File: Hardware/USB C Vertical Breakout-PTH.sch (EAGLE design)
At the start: 15 parts

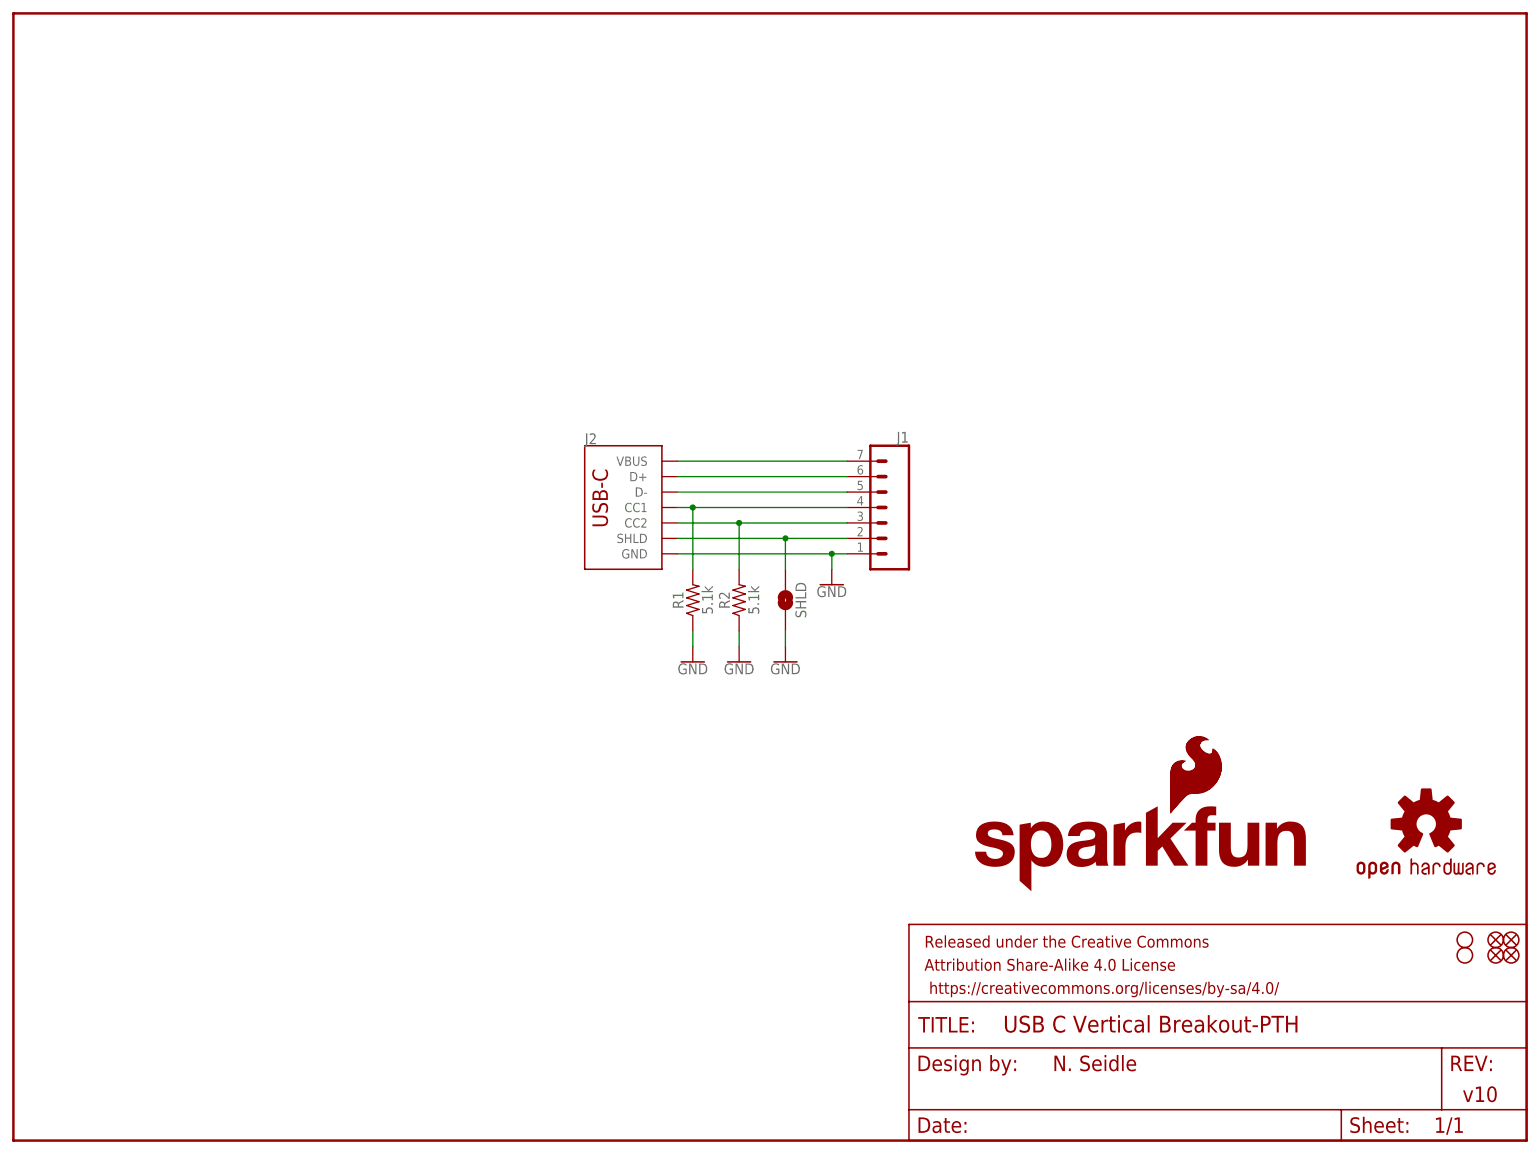
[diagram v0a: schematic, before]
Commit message: Repo Restructure, Work to board
Finished the new connector and the board layout; updates to schematic
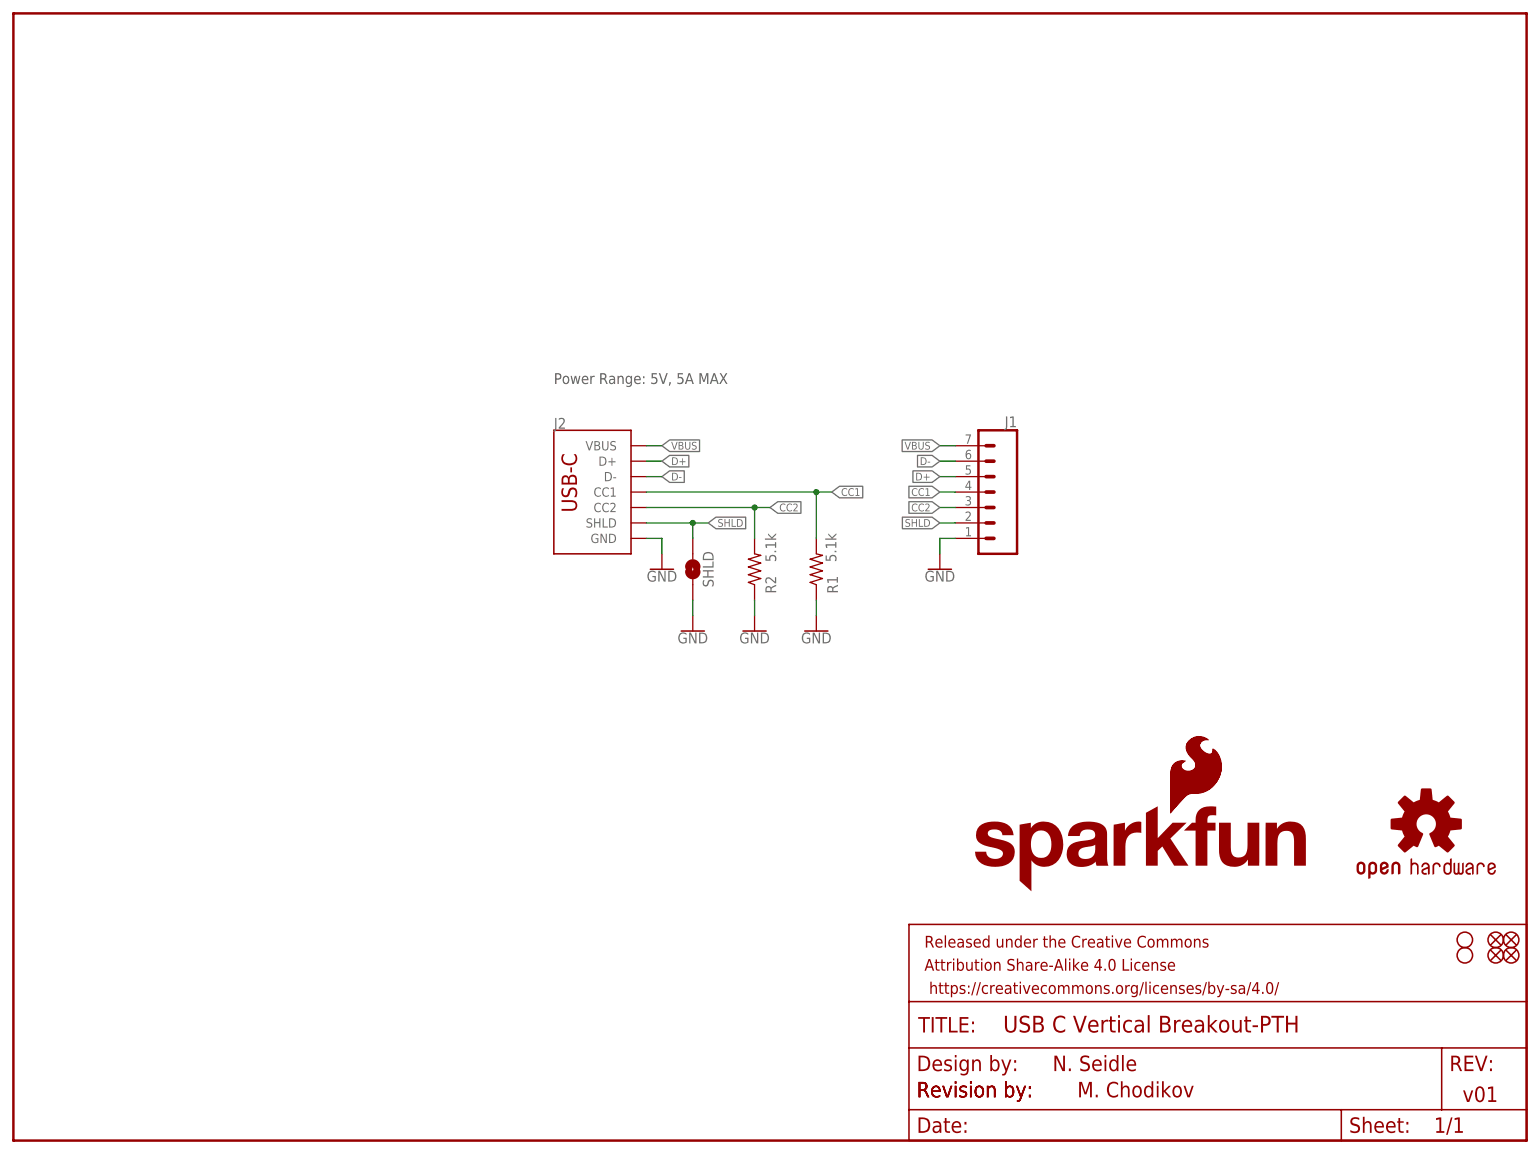
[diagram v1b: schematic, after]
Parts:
- J2: device USB C Vertical:USB_C_2-LAYER-VERTICAL-PTH -> USB-C_Vertical:USB_C_2-LAYER-VERTICAL-PTH
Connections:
- net D+: now also J1.5; no longer J1.6
- net D-: now also J1.6; no longer J1.5
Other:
- note added: "M. Chodikov"
- note added: "Power Range: 5V, 5A MAX"
- note added: "Revision by:"
- note added: "v01"
- note removed: "v10"
- moved on the sheet: J1, J2, R1, R2, SHLD

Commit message: Ready for Protos Design Review
Updated the README and the board/schematic files in preparation for the protos design review. The only schematic change was the comment and position of the aesthetics, and the board change was aesthetic.
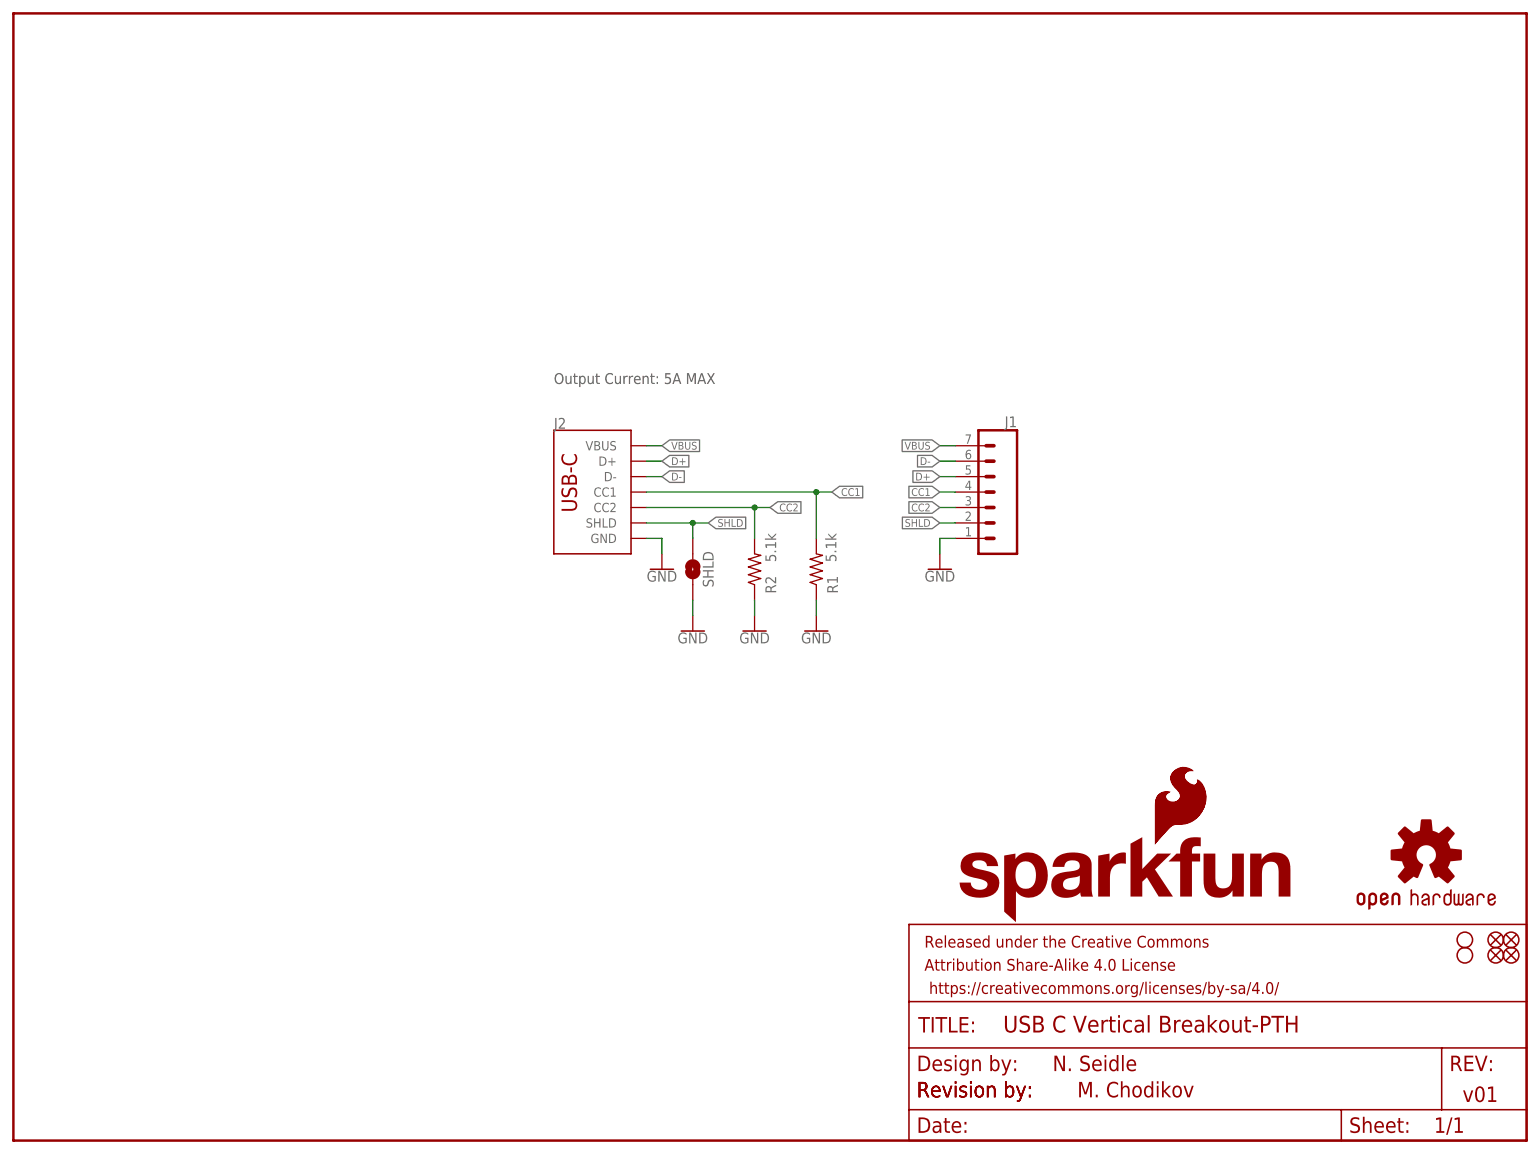
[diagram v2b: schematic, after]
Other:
- note added: "Output Current: 5A MAX"
- note removed: "Power Range: 5V, 5A MAX"
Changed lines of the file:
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@@
 <text x="148.59" y="7.112" size="2.54" layer="94">Revision by: </text>
 <text x="175.006" y="7.112" size="2.54" layer="94">M. Chodikov</text>
-<text x="88.9" y="124.46" size="1.778" layer="97">Power Range: 5V, 5A MAX</text>
+<text x="88.9" y="124.46" size="1.778" layer="97">Output Current: 5A MAX</text>
 </plain>
 <instances>
-<instance part="LOGO2" gate="G$1" x="232.41" y="52.07" smashed="yes"/>
+<instance part="LOGO2" gate="G$1" x="232.41" y="46.99" smashed="yes"/>
 <instance part="FD1" gate="G$1" x="246.38" y="33.02" smashed="yes"/>
 <instance part="FD2" gate="G$1" x="243.84" y="33.02" smashed="yes"/>
@@
 <instance part="H1" gate="G$1" x="238.76" y="33.02" smashed="yes"/>
 <instance part="H2" gate="G$1" x="238.76" y="30.48" smashed="yes"/>
-<instance part="LOGO1" gate="G$1" x="157.48" y="40.64" smashed="yes"/>
+<instance part="LOGO1" gate="G$1" x="154.94" y="35.56" smashed="yes"/>
 <instance part="FRAME2" gate="G$1" x="0" y="0" smashed="yes"/>
 <instance part="FRAME2" gate="V" x="147.32" y="0" smashed="yes">
@@
 <attribute name="VALUE" x="111.76" y="83.566" size="1.778" layer="96" font="vector" align="top-center"/>
 </instance>
-<instance part="LOGO3" gate="G$1" x="189.992" y="53.34" smashed="yes"/>
+<instance part="LOGO3" gate="G$1" x="187.452" y="48.26" smashed="yes"/>
 <instance part="R2" gate="R1" x="121.92" y="93.98" smashed="yes" rot="R90">
 <attribute name="NAME" x="125.476" y="91.44" size="1.778" layer="95" font="vector" rot="R90" align="bottom-center"/>

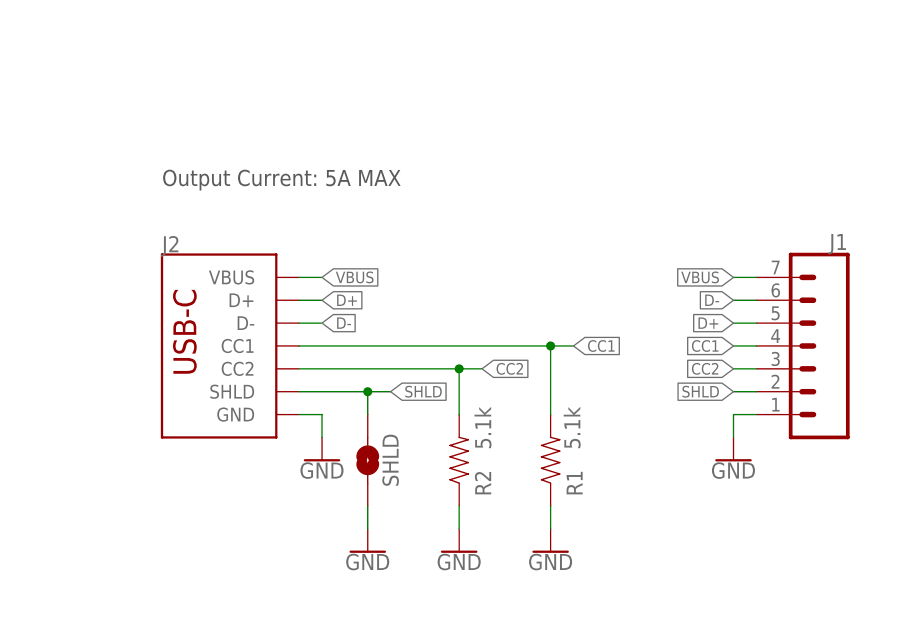
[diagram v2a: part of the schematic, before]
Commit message: PCB files ready for order
Made updates to schematic and layout as per the design review - see design review document for more detailed information. Added gerber files and BOM files for PCB assembly at JLC.
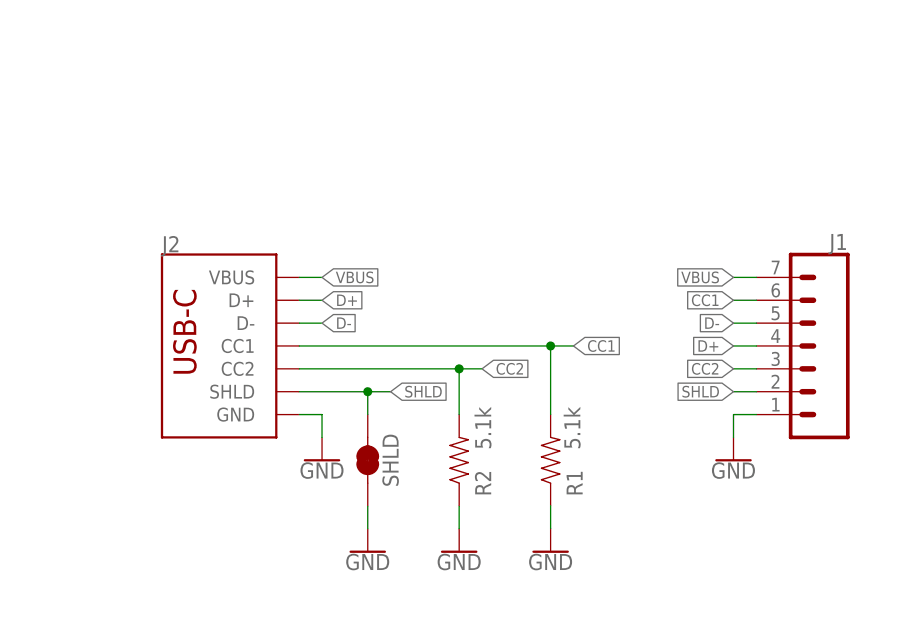
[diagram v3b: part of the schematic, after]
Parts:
- SHLD: device SparkFun-Jumpers:JUMPER-SMT_2_NO_NO-SILK -> SparkFun-Jumpers:JUMPER-SMT_2_NC_TRACE_NO-SILK
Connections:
- net CC1: now also J1.6; no longer J1.4
- net D+: now also J1.4; no longer J1.5
- net D-: now also J1.5; no longer J1.6
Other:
- note removed: "Output Current: 5A MAX"
